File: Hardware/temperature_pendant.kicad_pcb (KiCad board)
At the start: 2 copper layers, 22.2 x 36.3 mm, 15 parts, among them J1 CONN-6, J2 USB_MINI, SW1 SW-MOM, U1 MCP73831/2, U2 BLINKM/MINM, U3 TMP3X

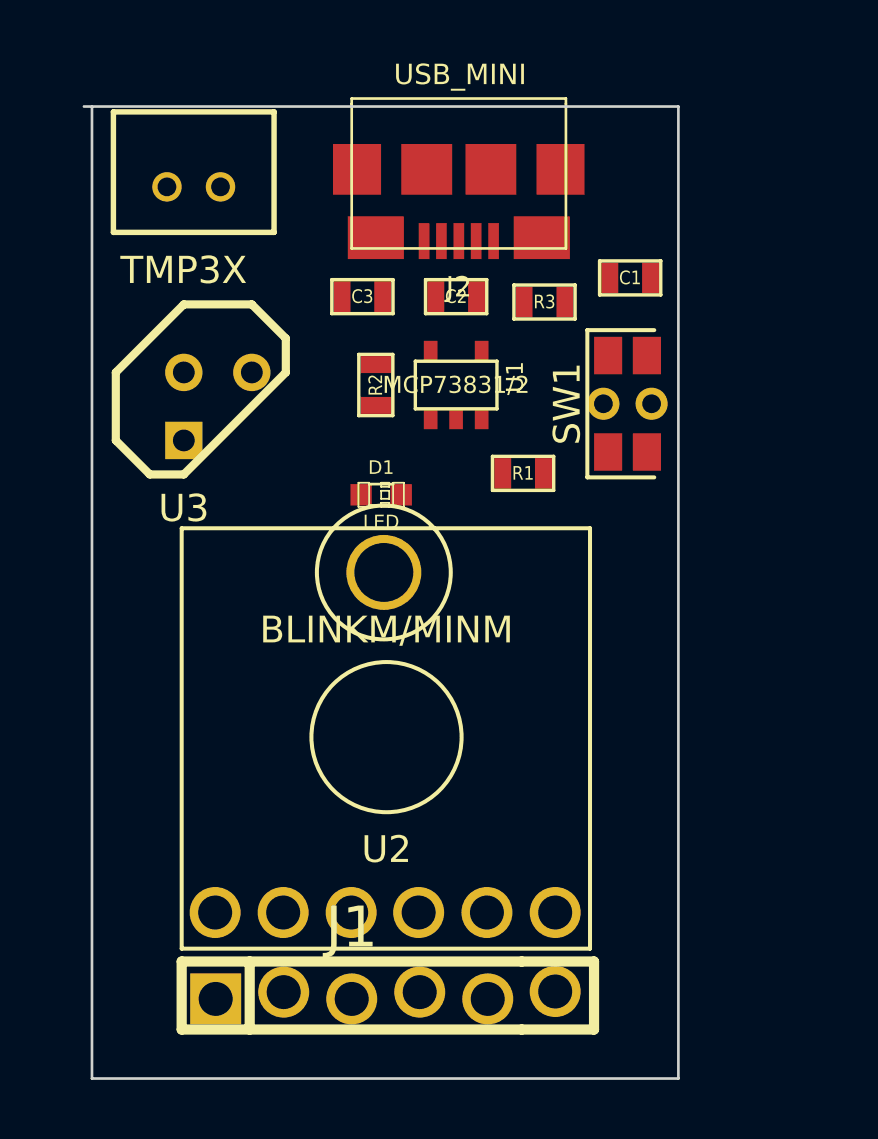
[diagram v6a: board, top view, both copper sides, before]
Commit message: Switched to MinM
Switched to MinM board in Master branch
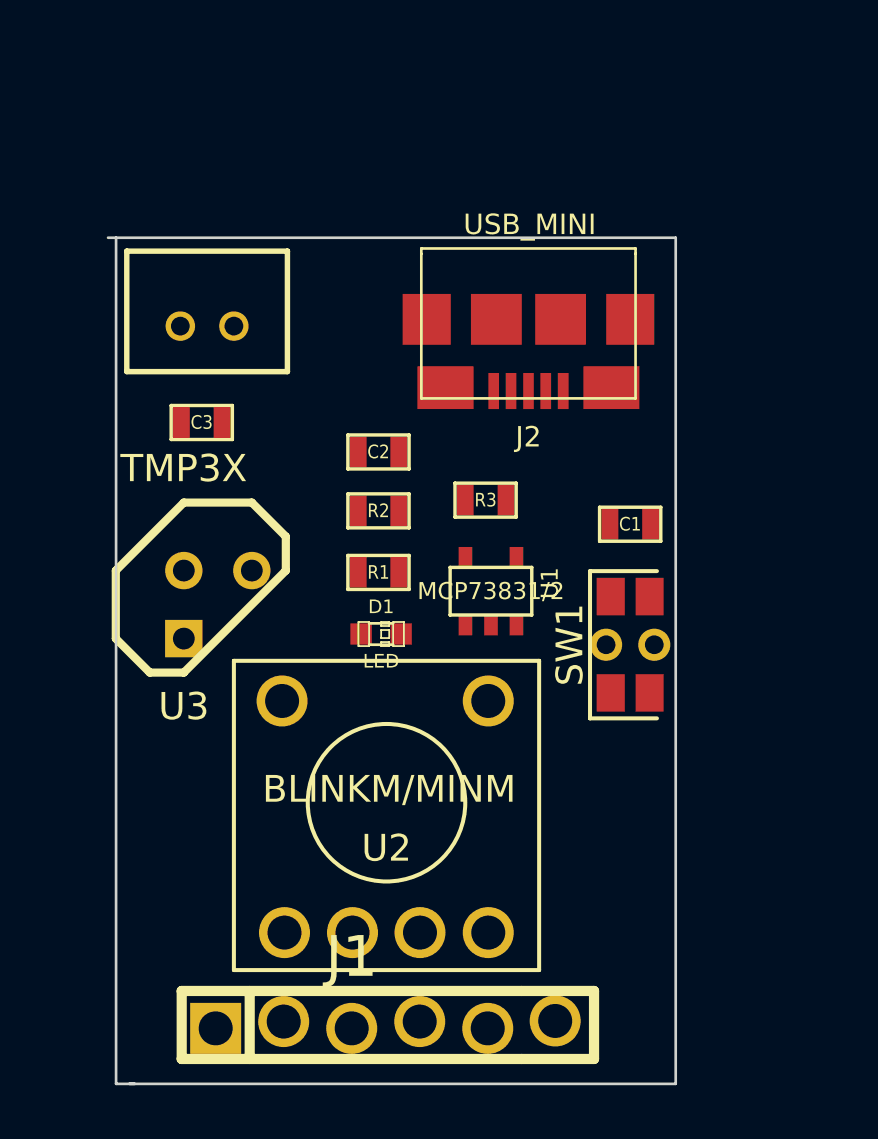
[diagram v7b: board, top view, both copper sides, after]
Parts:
- removed MECH-HOLE220: VAL**, MECH-HOLE220
- U2: footprint BlinkM -> MinM
- moved C1 9.20 mm to (219.6, 135.0)
- moved SW1 9.00 mm to (219.6, 139.5)
- moved U1 7.81 mm to (214.4, 137.5)
- moved R3 7.72 mm to (214.2, 134.1), turned to 180 degrees
- moved C3 7.62 mm to (203.6, 131.2), turned to 180 degrees
- moved U3 7.40 mm to (204.2, 138.0)
- moved R1 6.55 mm to (210.2, 136.8)
- moved C2 6.48 mm to (210.2, 132.3)
- moved J2 6.17 mm to (215.8, 125.9)
- moved BT1 5.22 mm to (203.8, 127.6)
- moved D1 5.20 mm to (210.3, 139.1)
- moved R2 4.70 mm to (210.2, 134.5), turned to 180 degrees
- moved U2 2.40 mm to (210.5, 145.4)
- moved J1 1.10 mm to (209.2, 153.7)
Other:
- board size 22.2 x 36.3 mm -> 21.2 x 31.6 mm
